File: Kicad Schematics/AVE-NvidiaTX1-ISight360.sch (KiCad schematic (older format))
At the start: 0 parts

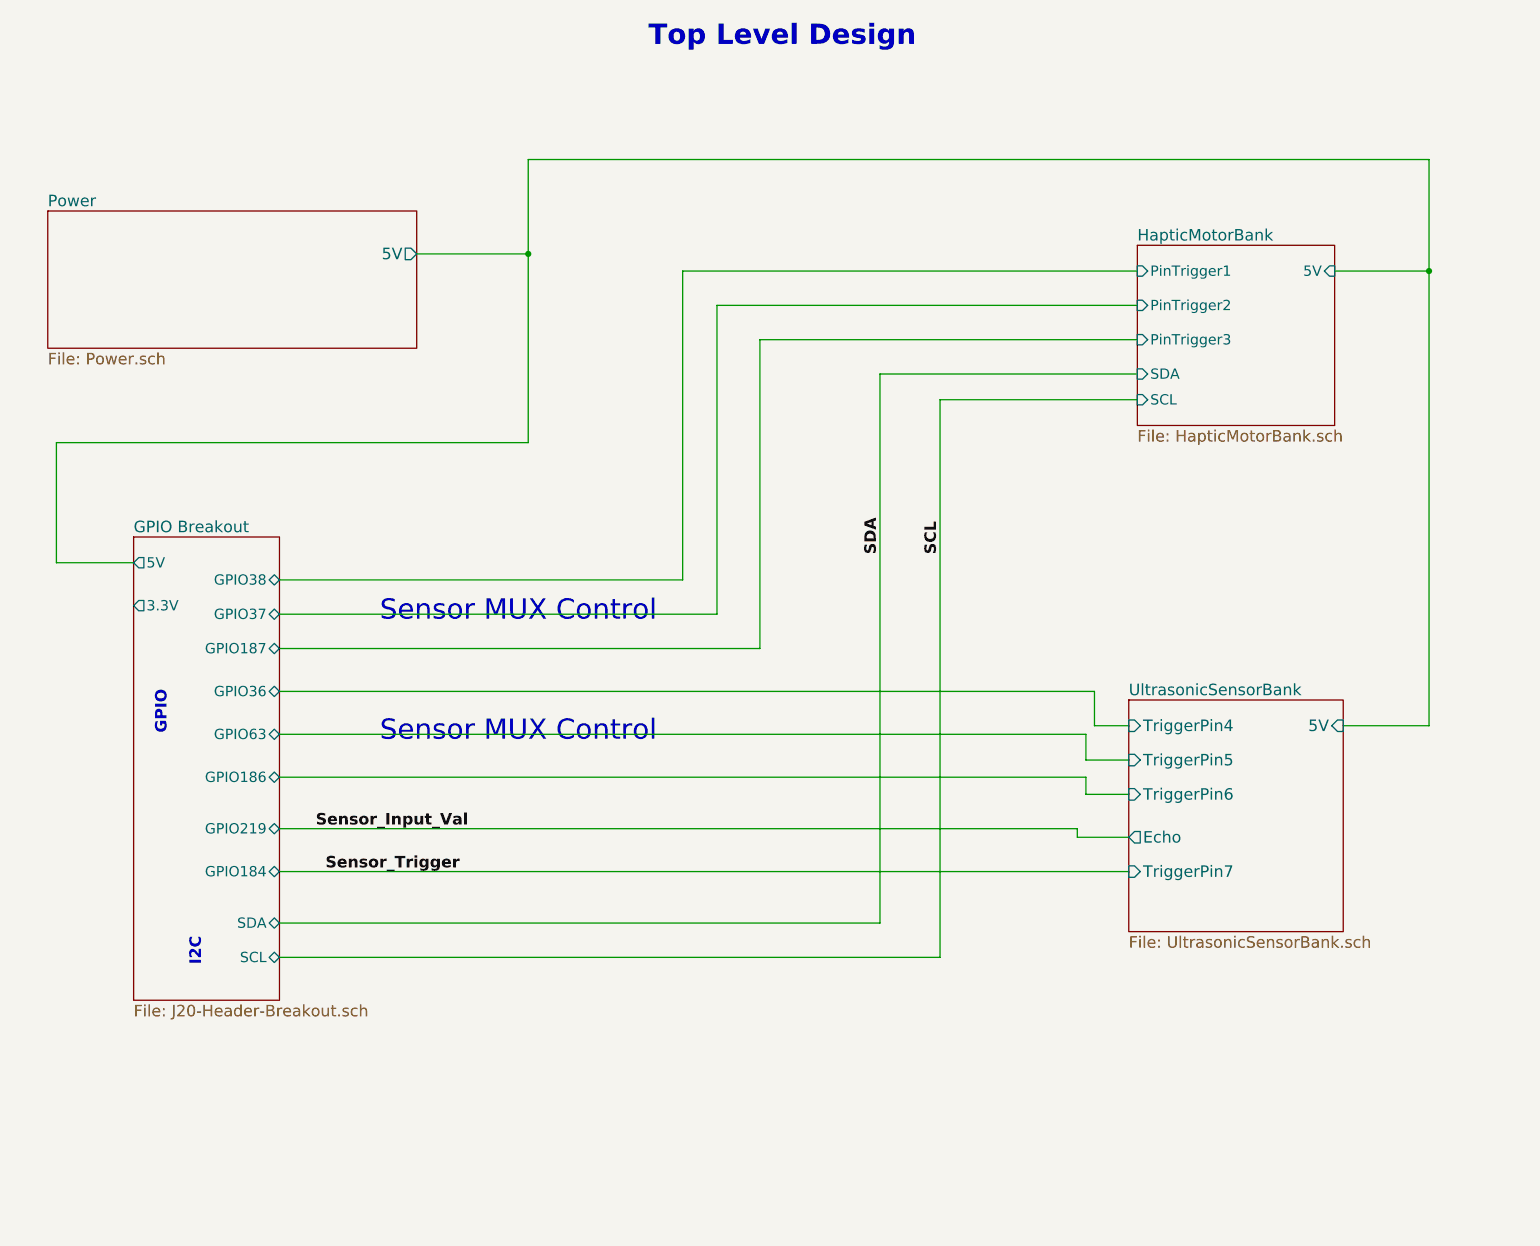
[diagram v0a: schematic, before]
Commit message: Reduced number of components
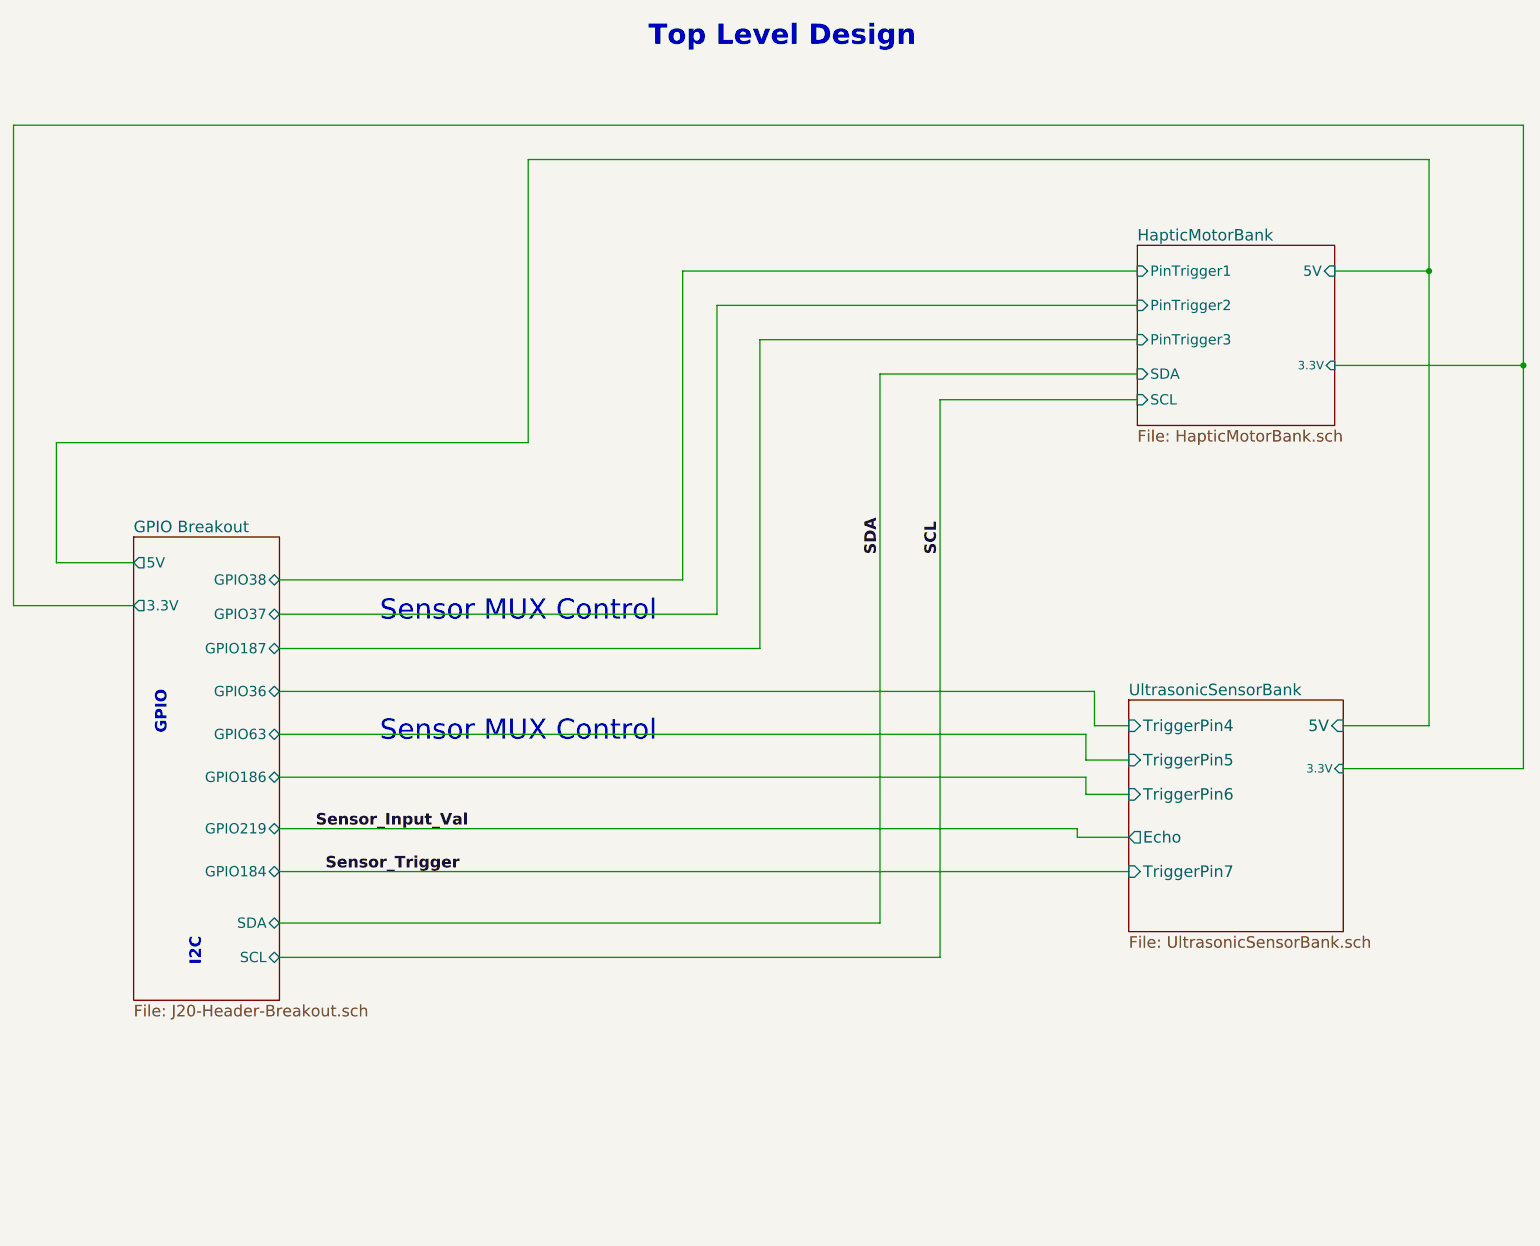
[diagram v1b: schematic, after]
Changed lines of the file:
@@
 $Descr A 11000 8500
 encoding utf-8
-Sheet 1 5
+Sheet 1 4
 Title "iSight360"
 Date "2017-03-17"
@@
 Comment4 ""
 $EndDescr
-$Sheet
-S 1300 2050 2150 800
-U 58CA7067
-F0 "Power" 67
-F1 "Power.sch" 67
-F2 "5V" O R 3450 2300 67
-$EndSheet
 $Sheet
 S 1800 3950 850  2700
@@
 F6 "PinTrigger3" I L 7650 2800 60
 F7 "PinTrigger1" I L 7650 2400 60
+F8 "3.3V" I R 8800 2950 49
 $EndSheet
 Wire Wire Line
@@
 	7300 5700 7600 5700
 Wire Wire Line
-	3450 2300 4100 2300
-Wire Wire Line
-	4100 1750 4100 3400
-Wire Wire Line
 	4100 1750 9350 1750
 Wire Wire Line
@@
 F6 "TriggerPin7" I L 7600 5900 67
 F7 "5V" I R 8850 5050 67
+F8 "3.3V" I R 8850 5300 49
 $EndSheet
 Text Notes 4800 1100 0    118  ~ 24
@@
 Wire Wire Line
 	1350 3400 4100 3400
-Connection ~ 4100 2300
+Wire Wire Line
+	1100 4350 1800 4350
+Wire Wire Line
+	4100 3400 4100 1750
+Wire Wire Line
+	1100 4350 1100 1550
+Wire Wire Line
+	1100 1550 9900 1550
+Wire Wire Line
+	9900 1550 9900 5300
+Wire Wire Line
+	9900 2950 8800 2950
+Wire Wire Line
+	9900 5300 8850 5300
+Connection ~ 9900 2950
 $EndSCHEMATC

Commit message: Rev C Update
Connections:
- net labels added: Echo1, Echo2, Echo3, Echo4, Echo5, Echo6, Mtrigger1, Mtrigger2, Mtrigger3, Mtrigger4, Mtrigger5, Mtrigger6, UltrasonicTigger, UltrasonicTrigger
- wire segments 42 -> 80
